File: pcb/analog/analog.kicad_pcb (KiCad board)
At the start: 2 copper layers, 70 x 70 mm, 68 parts, among them J1 USB_C_Receptacle_USB2.0, SW1 SW_Push, SW2 SW_Push, U1 SRV05-4, U2 XC6206P332MR, U3 DRV5056A3xDBZxQ1, U4 DRV5056A3xDBZxQ1, U5 DRV5056A3xDBZxQ1, U6 74AHCT1G125, U7 74AHCT1G125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

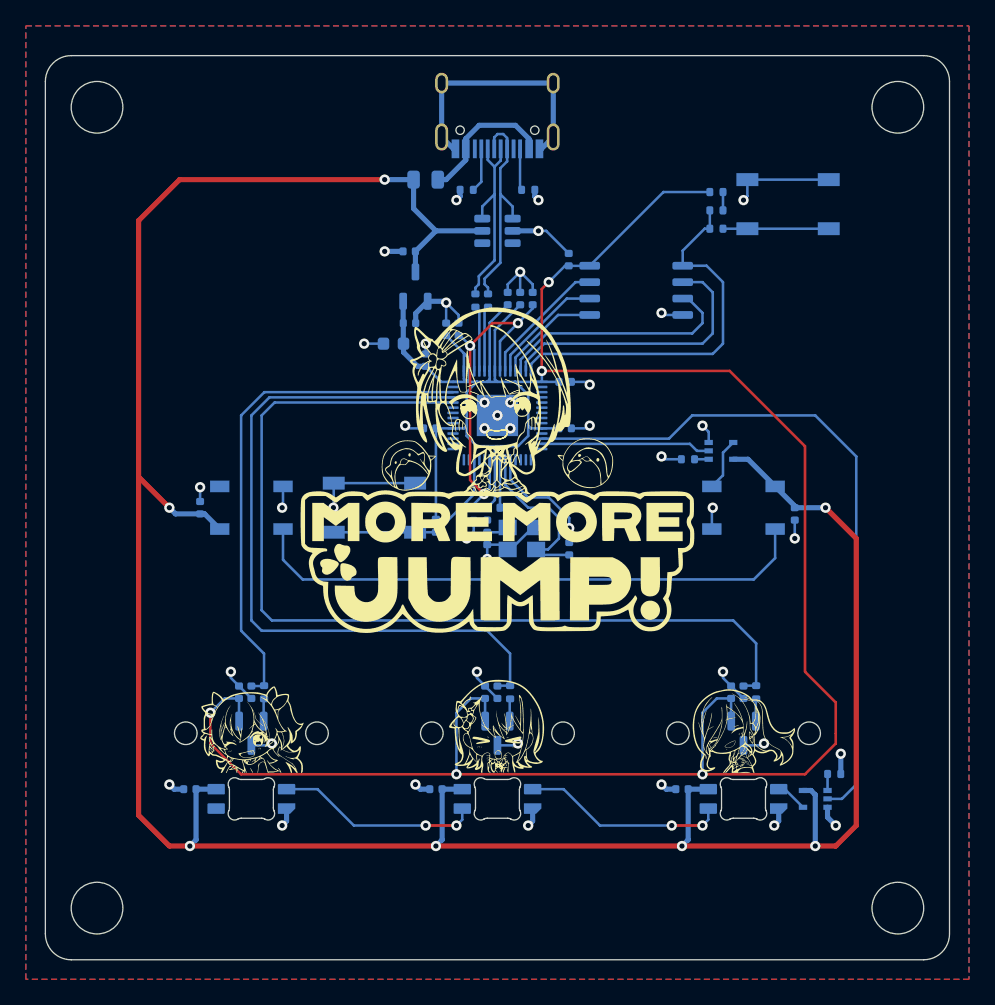
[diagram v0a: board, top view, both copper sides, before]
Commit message: chore: remove pcb artwork for now since I want to try re-routing the PCB again.
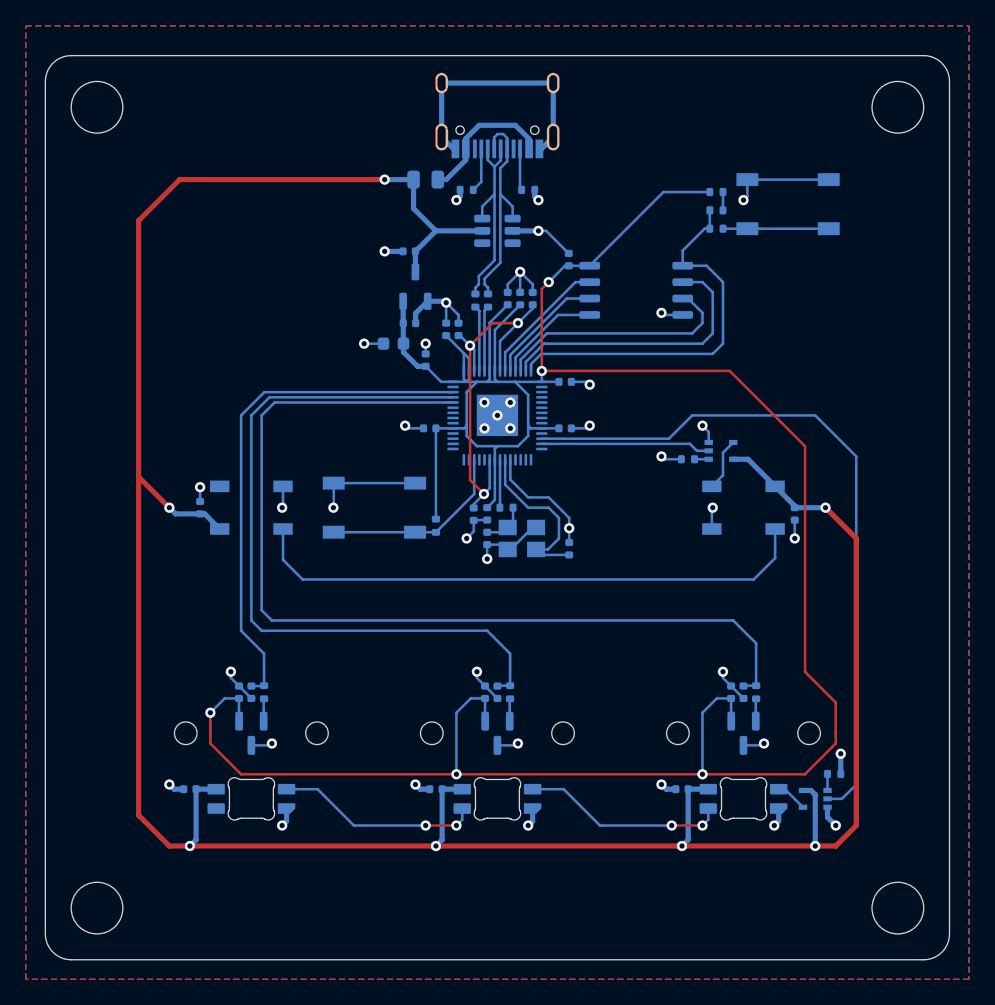
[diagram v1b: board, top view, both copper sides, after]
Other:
- board text removed: "Harukapad rev. 1 Designed by Ace4896"

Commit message: refactor: move mcu to top left
the routing is a lot more compact for the key components, and it looks like I'll have more room to route the relevant data lines.
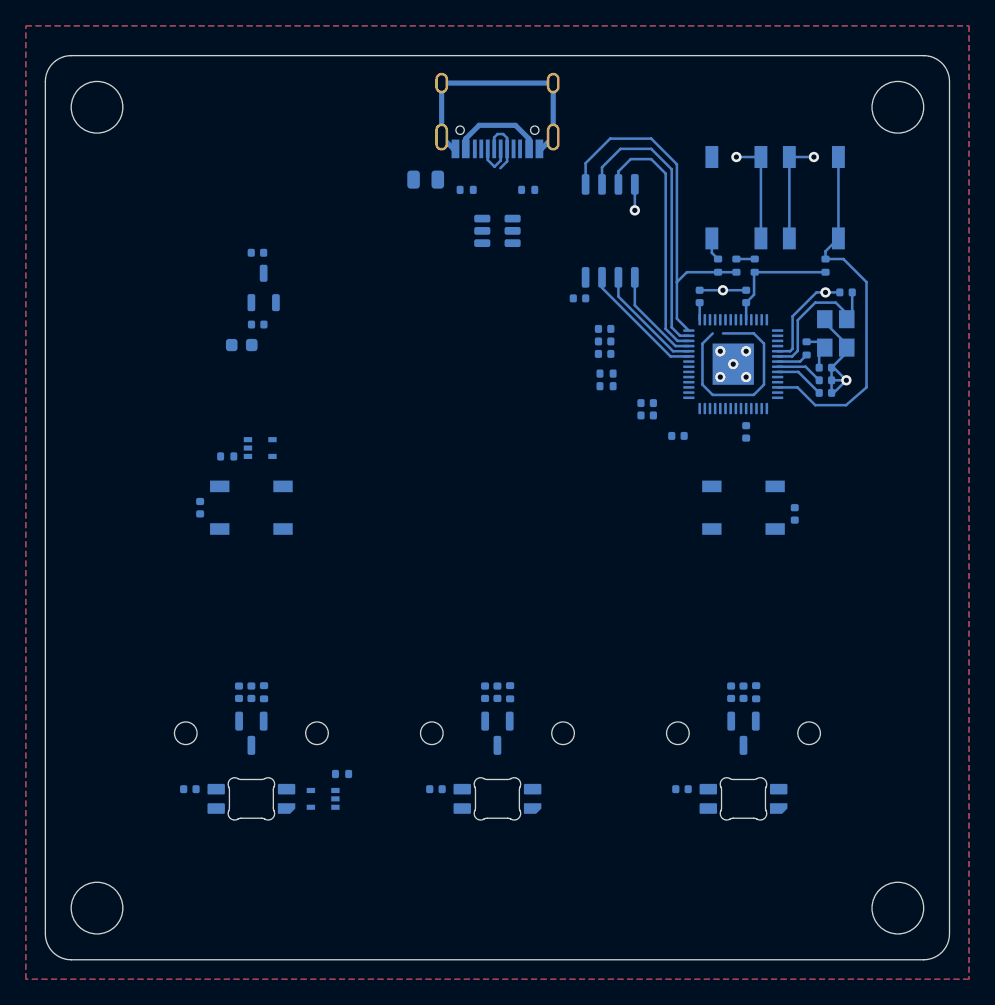
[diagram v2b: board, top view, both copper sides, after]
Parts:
- moved SW1 41.6 mm to (75.3, 26.8), turned to -90 degrees
- moved C11 38.1 mm to (65.1, 72.6)
- moved C9 38.1 mm to (27.0, 72.6)
- moved R3 38.1 mm to (32.7, 65.1)
- moved R5 38.1 mm to (70.8, 65.1)
- moved U6 38.1 mm to (37.3, 73.3)
- moved C1 38.1 mm to (30.8, 65.1)
- moved C3 38.1 mm to (68.9, 65.1)
- moved C6 38.1 mm to (31.8, 65.1)
- moved C8 38.1 mm to (69.8, 65.1)
- moved H1 38.1 mm to (31.8, 68.3)
- moved H3 38.1 mm to (69.8, 68.3)
- moved LED1 38.1 mm to (31.8, 73.3)
- moved LED3 38.1 mm to (69.8, 73.3)
- moved R6 38.1 mm to (38.8, 71.4)
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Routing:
- net +5V: track 203.8 -> 0.00 mm, vias 7 -> 0
- net +3V3: track 214.4 -> 14.4 mm, vias 5 -> 0
- net HS0: track 73.9 -> 0.00 mm
- net HS1: track 56.6 -> 0.00 mm
- net GND: track 116.8 -> 61.2 mm, vias 42 -> 11
- net RGB_HS: track 54.5 -> 0.00 mm
- net Net-(D1-DOUT): track 44.1 -> 0.00 mm
- net HS2: track 39.8 -> 0.00 mm
- net +1V1: track 30.1 -> 3.89 mm, vias 3 -> 0
- net (no net): track 0.00 -> 16.4 mm
- net Net-(LED2-DOUT): track 15.8 -> 0.00 mm, vias 2 -> 0
- net Net-(LED1-DOUT): track 15.8 -> 0.00 mm, vias 2 -> 0
- net RESET: track 14.8 -> 28.3 mm
- net RGB_GLOW: track 13.1 -> 0.00 mm
- net D-: track 15.9 -> 3.18 mm
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
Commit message: refactor: new pcb layout
more compact and has fewer crossing lines. can definitely shrink the PCB, but I've picked this size so it's possible to see the design from the top.
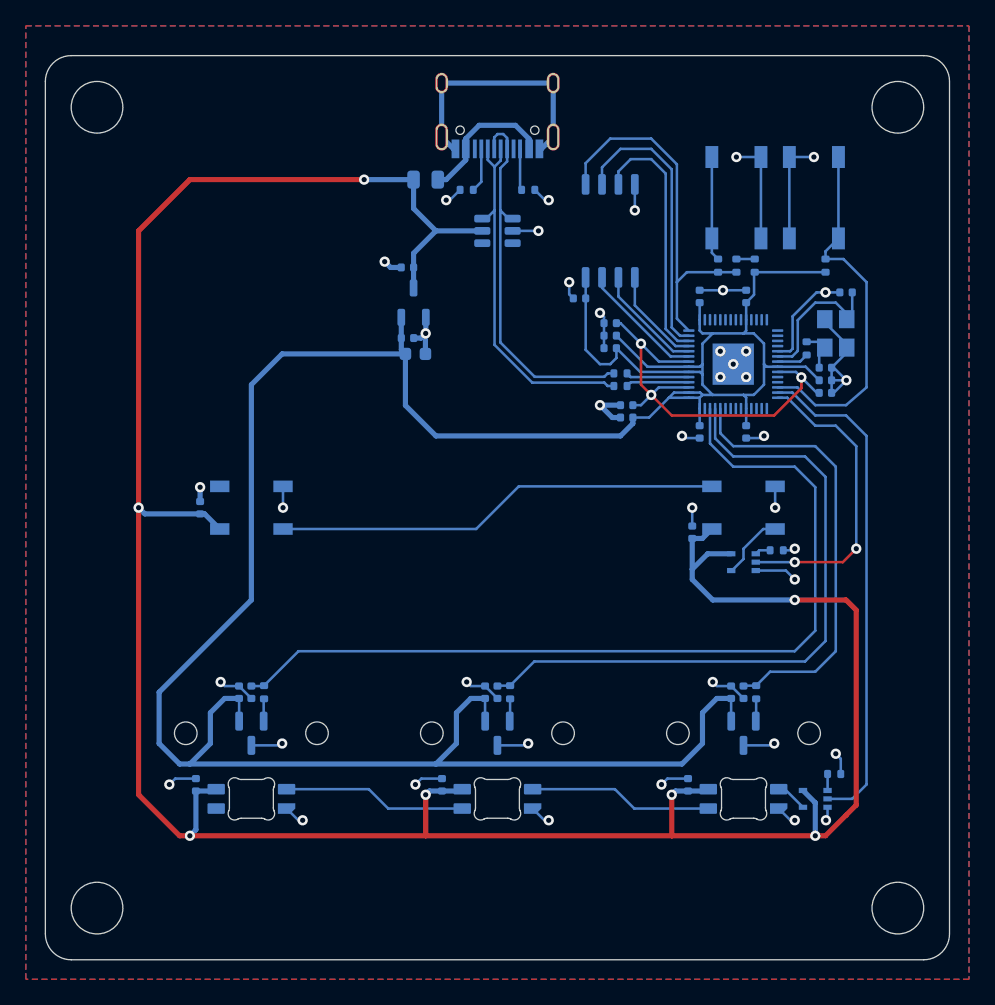
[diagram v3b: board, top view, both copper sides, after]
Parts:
- moved R8 43.2 mm to (72.4, 54.1), turned to 0 degrees
- moved C9 38.6 mm to (65.6, 72.3), turned to -90 degrees
- moved U7 38.4 mm to (69.8, 55.0), turned to 180 degrees
- moved R3 38.1 mm to (70.8, 65.1)
- moved R5 38.1 mm to (32.7, 65.1)
- moved U6 38.1 mm to (75.4, 73.3)
- moved C1 38.1 mm to (68.9, 65.1)
- moved C3 38.1 mm to (30.8, 65.1)
- moved C6 38.1 mm to (69.8, 65.1)
- moved C8 38.1 mm to (31.8, 65.1)
- moved H1 38.1 mm to (69.8, 68.3)
- moved H3 38.1 mm to (31.8, 68.3)
- moved LED1 38.1 mm to (69.8, 73.3)
- moved LED3 38.1 mm to (31.8, 73.3)
- moved R6 38.1 mm to (76.9, 71.4)
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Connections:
- U8 pad 12: RGB_HS -> unconnected-(U8-GPIO9-Pad12)
- U8 pad 13: RGB_GLOW -> unconnected-(U8-GPIO10-Pad13)
- U8 pad 27: unconnected-(U8-GPIO16-Pad27) -> RGB_HS
- U8 pad 28: unconnected-(U8-GPIO17-Pad28) -> RGB_GLOW
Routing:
- net +5V: track 0.00 -> 203.7 mm, vias 0 -> 7
- net +3V3: track 14.4 -> 213.2 mm
- net HS2: track 0.00 -> 68.8 mm
- net GND: track 61.2 -> 122.6 mm, vias 11 -> 41
- net HS1: track 0.00 -> 51.6 mm
- net RGB_HS: track 0.00 -> 38.7 mm
- net Net-(D1-DOUT): track 0.00 -> 34.6 mm
- net HS0: track 0.00 -> 34.5 mm
- net +1V1: track 3.89 -> 33.9 mm, vias 0 -> 3
- net D-: track 3.18 -> 28.7 mm
- net D+: track 4.68 -> 29.4 mm
- net RGB_GLOW: track 0.00 -> 23.8 mm, vias 0 -> 2
- net (no net): track 16.4 -> 0.00 mm
- net Net-(LED2-DOUT): track 0.00 -> 14.2 mm
- net Net-(LED1-DOUT): track 0.00 -> 14.2 mm
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
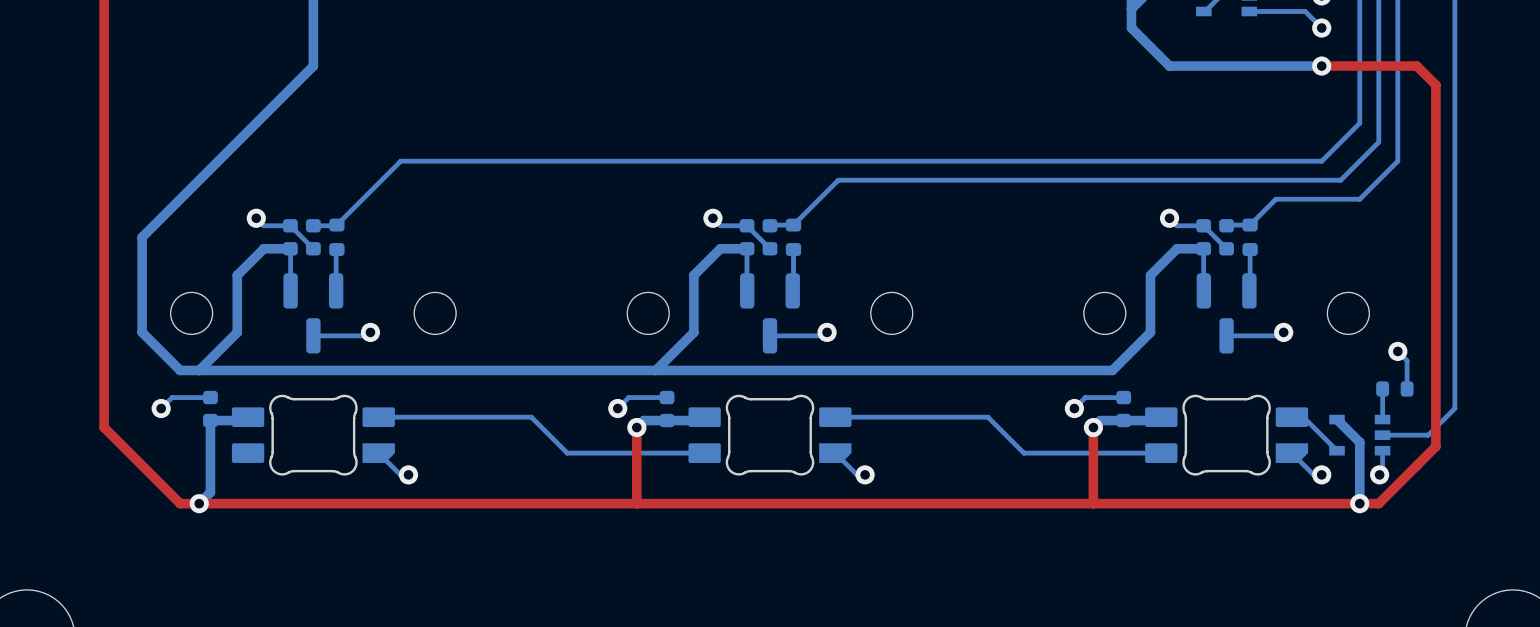
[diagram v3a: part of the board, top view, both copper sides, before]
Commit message: refactor: create custom footprint for KS-20 w/ DRV5056
this includes a custom silkscreen, reference value and a rule area to disallow copper fills in the middle of the sensor.
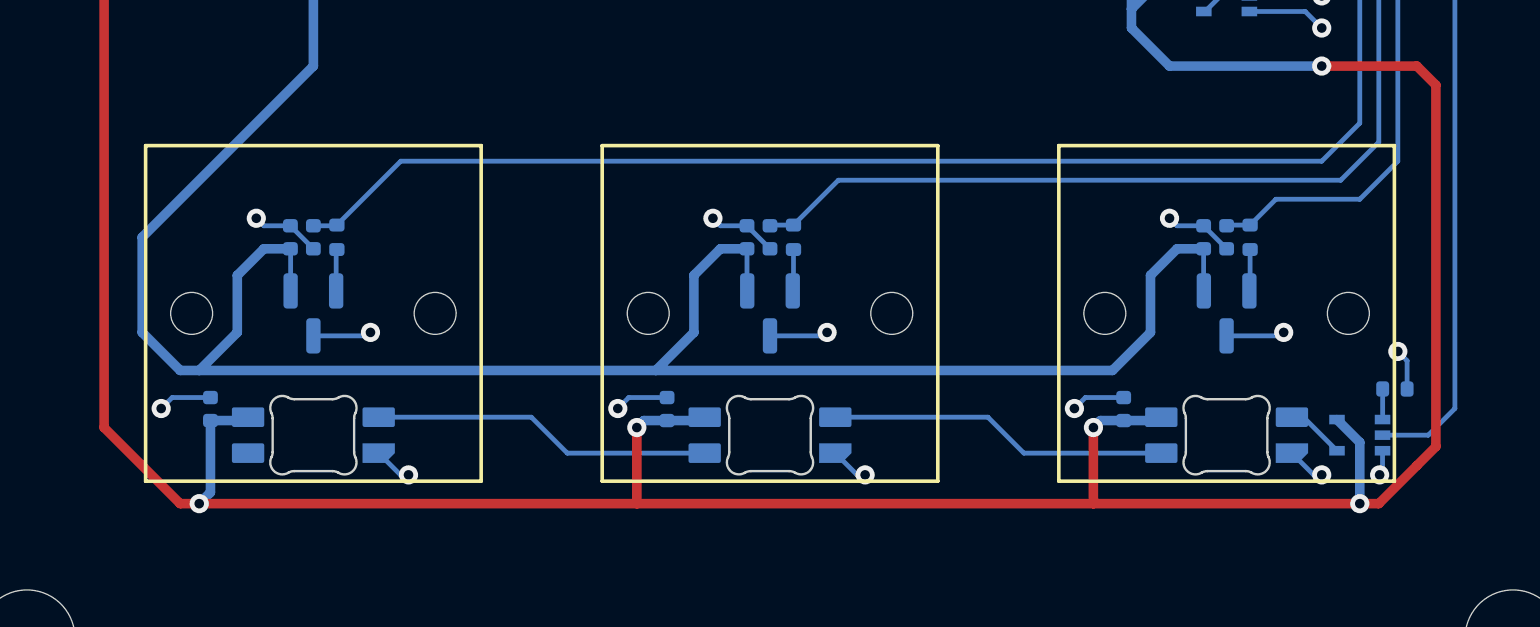
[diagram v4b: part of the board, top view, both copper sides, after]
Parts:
- removed H5, H6, H7: 4mm Mounting Hole, MountingHole:MountingHole_4mm
- H1, H2, H3: value Gateron KS-20 -> 4mm Mounting Hole; footprint Custom:MX-1U-NoPins -> MountingHole:MountingHole_4mm; moved to F.Cu
- H4: moved to F.Cu
- U3, U4, U5: footprint Package_TO_SOT_SMD:SOT-23 -> Custom:KS-20-1U-DRV5056; moved to F.Cu
- moved H4 87.7 mm to (81.8, 81.8), turned to 0 degrees
- moved H1 69.7 mm to (19.8, 19.8), turned to 0 degrees
- moved H2 57.5 mm to (81.8, 19.8), turned to 0 degrees
- moved H3 18.1 mm to (19.8, 81.8), turned to 0 degrees
- turned U3 to 0 degrees
- turned U4 to 0 degrees
- turned U5 to 0 degrees
